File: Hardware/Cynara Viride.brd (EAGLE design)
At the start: 160 x 100 mm, 197 parts, among them Q1 TXC-7B, Q2 TXC-7WNEO, SW1 430181038816, SW2 , T1 PDTC143, T2 PDTC143, T3 PDTC143, T4 PDTC143, T5 PDTC143, U1 TM4C129EN, U2 MCP1826S 3V3, U3 LM4132 3V3, U4 XC6SLX9-3TQG, U5 M25P16-SO8, U6 MCP1826S 1V2, X1 EDGE 50p, X11 SOCK2X17, X12 SOCK2X17, X13 SOCK2X17, X2 EDGE 50p, X23 debug xilinx, X24 debug 10p, X3 EDGE 50p, X4 EDGE 50p, X5 MicroMatch 24, X6 , X7 SOCK2X17, X8 RJ45-LAN-10/100

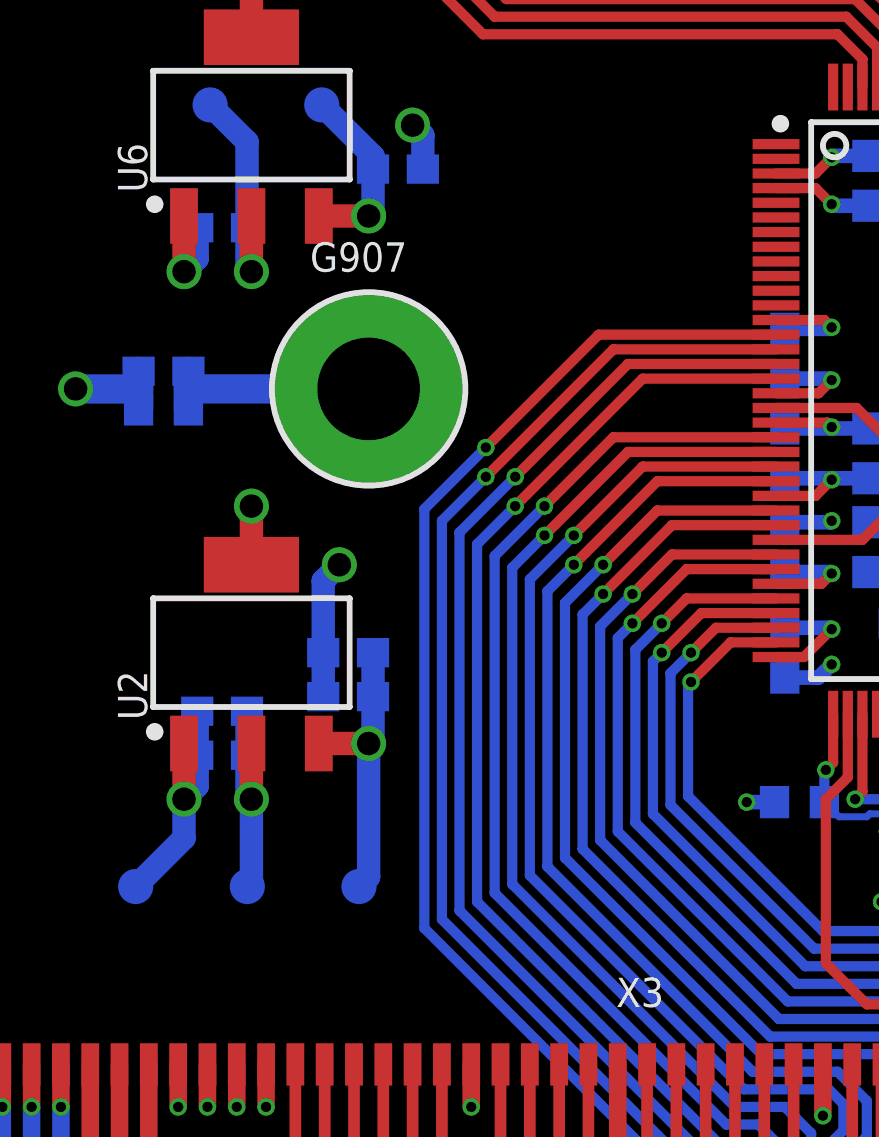
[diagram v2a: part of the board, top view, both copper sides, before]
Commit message: Added jumpers to disconnect the different power rails.
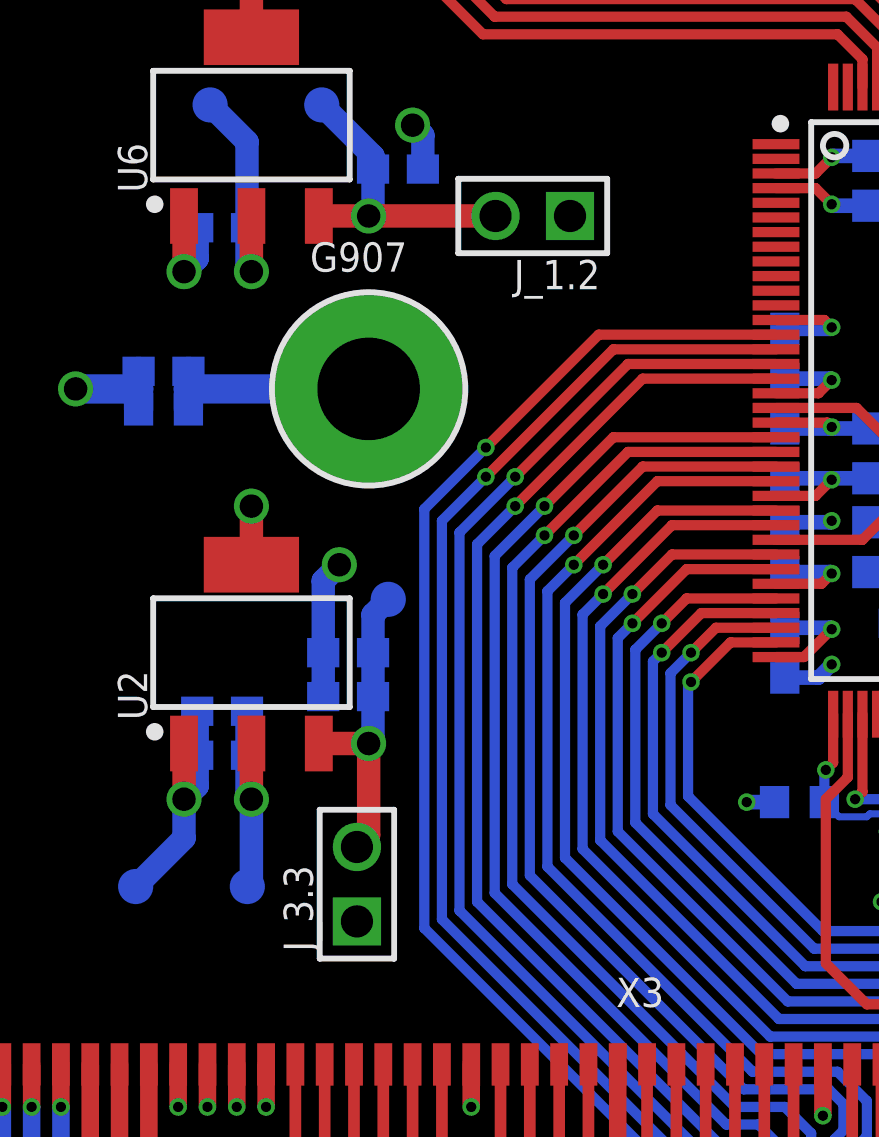
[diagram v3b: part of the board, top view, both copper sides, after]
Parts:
- added J_1.2, J_3.3: HDR1X2, Cynara-Connectors:1X2
- moved TP2 9.85 mm to (27.7, 42.8)
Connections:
- new net N$10: C44.1, J_1.2.2, TP3.1, U6.3
- new net N$7: C18.1, C57.1, J_3.3.2, TP2.1, U2.3
- net +1.2V: now also J_1.2.1; no longer C44.1, TP3.1, U6.3
- net +3.3V: now also J_3.3.1; no longer C18.1, C57.1, TP2.1, U2.3
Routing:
- net +1.2V: track 58.4 -> 44.6 mm, vias 5 -> 4
- net N$10: track 0.00 -> 10.6 mm, vias 0 -> 1
- net N$7: track 0.00 -> 10.6 mm, vias 0 -> 1
- net +3.3V: track 284.5 -> 274.6 mm, vias 49 -> 48
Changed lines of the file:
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@@
 <attribute name="XTRA" value="" x="19.05" y="33.02" size="1.778" layer="28" rot="MR0" display="off"/>
 </element>
-<element name="TP2" library="Cynara-Misc" package="TP-SMD" value=" " x="26.67" y="33.02" rot="MR0">
-<attribute name="Z" value="" x="26.67" y="33.02" size="1.778" layer="28" rot="MR0" display="off"/>
-<attribute name="WAARDE" value="" x="26.67" y="33.02" size="1.778" layer="28" rot="MR0" display="off"/>
-<attribute name="BEHUIZING" value="TP-EZ" x="26.67" y="33.02" size="1.778" layer="28" rot="MR0" display="off"/>
-<attribute name="ARTIKEL" value="" x="26.67" y="33.02" size="1.778" layer="28" rot="MR0" display="off"/>
-<attribute name="XTRA" value="" x="26.67" y="33.02" size="1.778" layer="28" rot="MR0" display="off"/>
+<element name="TP2" library="Cynara-Misc" package="TP-SMD" value=" " x="27.67" y="42.82" rot="MR0">
+<attribute name="Z" value="" x="27.67" y="42.82" size="1.778" layer="28" rot="MR0" display="off"/>
+<attribute name="WAARDE" value="" x="27.67" y="42.82" size="1.778" layer="28" rot="MR0" display="off"/>
+<attribute name="BEHUIZING" value="TP-EZ" x="27.67" y="42.82" size="1.778" layer="28" rot="MR0" display="off"/>
+<attribute name="ARTIKEL" value="" x="27.67" y="42.82" size="1.778" layer="28" rot="MR0" display="off"/>
+<attribute name="XTRA" value="" x="27.67" y="42.82" size="1.778" layer="28" rot="MR0" display="off"/>
 </element>
 <element name="TP3" library="Cynara-Misc" package="TP-SMD" value=" " x="25.4" y="59.69" rot="MR0">
@@
 <attribute name="MANUFACTURER" value="Texas Instruments" x="98.6" y="50" size="1.778" layer="27" rot="R315" display="off"/>
 </element>
+<element name="J_3.3" library="Cynara-Connectors" package="1X2" value="HDR1X2" x="26.6" y="33.1" rot="R90">
+<attribute name="MANUFACTURERPARTNO" value="61300211121" x="26.6" y="33.1" size="1.778" layer="27" rot="R90" display="off"/>
+<attribute name="MANUFACTURER" value="Wurth" x="26.6" y="33.1" size="1.778" layer="27" rot="R90" display="off"/>
+<attribute name="ORDERCODE" value="" x="26.6" y="33.1" size="1.778" layer="27" rot="R90" display="off"/>
+<attribute name="SUPPLIER" value="" x="26.6" y="33.1" size="1.778" layer="27" rot="R90" display="off"/>
+</element>
+<element name="J_1.2" library="Cynara-Connectors" package="1X2" value="HDR1X2" x="32.6" y="55.9" rot="R180">
+<attribute name="MANUFACTURERPARTNO" value="61300211121" x="32.6" y="55.9" size="1.778" layer="27" rot="R180" display="off"/>
+<attribute name="MANUFACTURER" value="Wurth" x="32.6" y="55.9" size="1.778" layer="27" rot="R180" display="off"/>
+<attribute name="ORDERCODE" value="" x="32.6" y="55.9" size="1.778" layer="27" rot="R180" display="off"/>
+<attribute name="SUPPLIER" value="" x="32.6" y="55.9" size="1.778" layer="27" rot="R180" display="off"/>
+</element>
 </elements>
 <signals>
@@
 <contactref element="C42" pad="1"/>
 <contactref element="L2" pad="2"/>
-<contactref element="C57" pad="1"/>
 <contactref element="R13" pad="2"/>
 <contactref element="C58" pad="1"/>
@@
 <wire x1="75.83" y1="16.3" x2="74" y2="18.13" width="0.35" layer="16"/>
 <wire x1="74" y1="18.13" x2="74" y2="24.2" width="0.35" layer="16"/>
-<contactref element="U2" pad="3"/>
-<contactref element="C18" pad="1"/>
 <contactref element="C61" pad="1"/>
 <contactref element="C62" pad="1"/>
@@
 <via x="80.6" y="36" extent="1-16" drill="0.35"/>
 <via x="44.7" y="34.9" extent="1-16" drill="0.35"/>
-<wire x1="25.3" y1="37.9" x2="27" y2="37.9" width="0.8" layer="1"/>
-<via x="27" y="37.9" extent="1-16" drill="0.8"/>
-<wire x1="27.15" y1="41" x2="27.15" y2="39.5" width="0.8" layer="16"/>
-<wire x1="27.15" y1="39.5" x2="27.15" y2="38.05" width="0.8" layer="16"/>
-<wire x1="27.15" y1="38.05" x2="27" y2="37.9" width="0.8" layer="16"/>
 <wire x1="46.46" y1="35.6" x2="45.4" y2="35.6" width="0.5" layer="1"/>
 <wire x1="45.4" y1="35.6" x2="44.7" y2="34.9" width="0.5" layer="1"/>
@@
 <wire x1="151" y1="78.15" x2="150.85" y2="78" width="0.35" layer="16"/>
 <wire x1="150.85" y1="78" x2="148" y2="78" width="0.35" layer="16"/>
-<contactref element="TP2" pad="1"/>
-<wire x1="26.67" y1="33.02" x2="27" y2="33.35" width="0.8" layer="16"/>
-<wire x1="27" y1="33.35" x2="27" y2="37.9" width="0.8" layer="16"/>
 <contactref element="U1" pad="7"/>
 <contactref element="U1" pad="16"/>
@@
 <wire x1="90.81715625" y1="57.5" x2="90.5" y2="57.5" width="0.24" layer="1"/>
 <via x="90.5" y="57.5" extent="1-16" drill="0.35"/>
+<contactref element="J_3.3" pad="1"/>
 </signal>
 <signal name="M0">
@@
 <vertex x="48" y="42"/>
 </polygon>
-<contactref element="U6" pad="3"/>
-<contactref element="C44" pad="1"/>
 <wire x1="62.3" y1="48.85" x2="61.35" y2="48.85" width="0.35" layer="1"/>
 <wire x1="61.35" y1="48.85" x2="61" y2="48.5" width="0.35" layer="1"/>
@@
 <wire x1="43.65" y1="49.35" x2="45.5" y2="47.5" width="0.35" layer="1"/>
 <wire x1="45.5" y1="47.5" x2="45.5" y2="46.5" width="0.35" layer="1"/>
-<wire x1="25.3" y1="55.9" x2="27" y2="55.9" width="0.8" layer="1"/>
-<via x="27" y="55.9" extent="1-16" drill="0.8"/>
-<wire x1="27.15" y1="57.5" x2="27.15" y2="56.05" width="0.8" layer="16"/>
-<wire x1="27.15" y1="56.05" x2="27" y2="55.9" width="0.8" layer="16"/>
-<wire x1="27" y1="55.9" x2="41.1" y2="55.9" width="0.8" layer="15"/>
-<wire x1="41.1" y1="55.9" x2="44" y2="53" width="0.8" layer="15"/>
-<contactref element="TP3" pad="1"/>
-<wire x1="25.4" y1="59.69" x2="27.15" y2="57.94" width="0.8" layer="16"/>
-<wire x1="27.15" y1="57.94" x2="27.15" y2="57.5" width="0.8" layer="16"/>
+<contactref element="J_1.2" pad="1"/>
+<wire x1="33.87" y1="55.9" x2="41" y2="55.9" width="0.8" layer="15"/>
+<wire x1="41" y1="55.9" x2="43.5" y2="53.4" width="0.8" layer="15"/>
 </signal>
 <signal name="X3V3">
@@
 <wire x1="102.7" y1="58.908328125" x2="102.7" y2="59" width="0.24" layer="1"/>
 </signal>
+<signal name="N$7">
+<contactref element="C57" pad="1"/>
+<contactref element="U2" pad="3"/>
+<contactref element="C18" pad="1"/>
+<contactref element="TP2" pad="1"/>
+<contactref element="J_3.3" pad="2"/>
+<wire x1="25.3" y1="37.9" x2="27" y2="37.9" width="0.8" layer="1"/>
+<via x="27" y="37.9" extent="1-16" drill="0.8"/>
+<wire x1="27.15" y1="41" x2="27.15" y2="39.5" width="0.8" layer="16"/>
+<wire x1="27.15" y1="39.5" x2="27.15" y2="38.05" width="0.8" layer="16"/>
+<wire x1="27.15" y1="38.05" x2="27" y2="37.9" width="0.8" layer="16"/>
+<wire x1="26.6" y1="34.37" x2="27" y2="34.77" width="0.8" layer="1"/>
+<wire x1="27" y1="34.77" x2="27" y2="37.9" width="0.8" layer="1"/>
+<wire x1="27.15" y1="41" x2="27.15" y2="42.3" width="0.8" layer="16"/>
+<wire x1="27.15" y1="42.3" x2="27.67" y2="42.82" width="0.8" layer="16"/>
+</signal>
+<signal name="N$10">
+<contactref element="U6" pad="3"/>
+<contactref element="C44" pad="1"/>
+<contactref element="TP3" pad="1"/>
+<contactref element="J_1.2" pad="2"/>
+<wire x1="25.3" y1="55.9" x2="27" y2="55.9" width="0.8" layer="1"/>
+<via x="27" y="55.9" extent="1-16" drill="0.8"/>
+<wire x1="27.15" y1="57.5" x2="27.15" y2="56.05" width="0.8" layer="16"/>
+<wire x1="27.15" y1="56.05" x2="27" y2="55.9" width="0.8" layer="16"/>
+<wire x1="25.4" y1="59.69" x2="27.15" y2="57.94" width="0.8" layer="16"/>
+<wire x1="27.15" y1="57.94" x2="27.15" y2="57.5" width="0.8" layer="16"/>
+<wire x1="31.33" y1="55.9" x2="27" y2="55.9" width="0.8" layer="1"/>
+</signal>
 </signals>

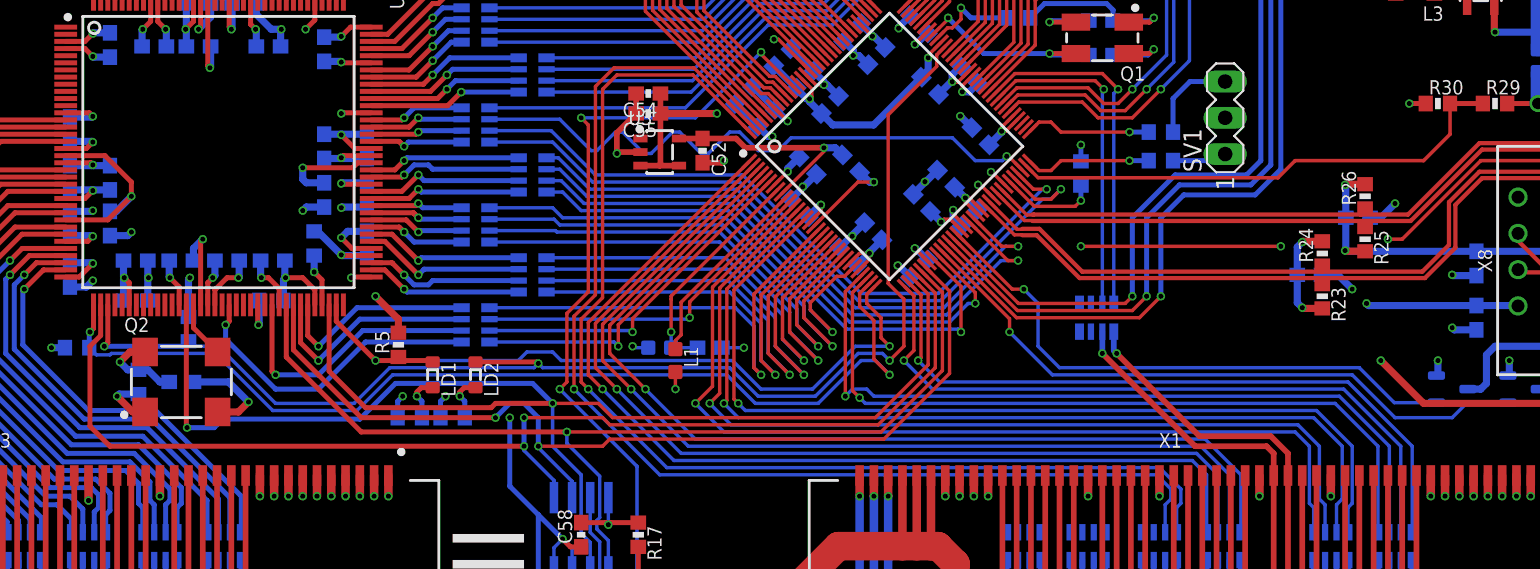
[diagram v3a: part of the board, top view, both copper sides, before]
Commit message: Added more test points.
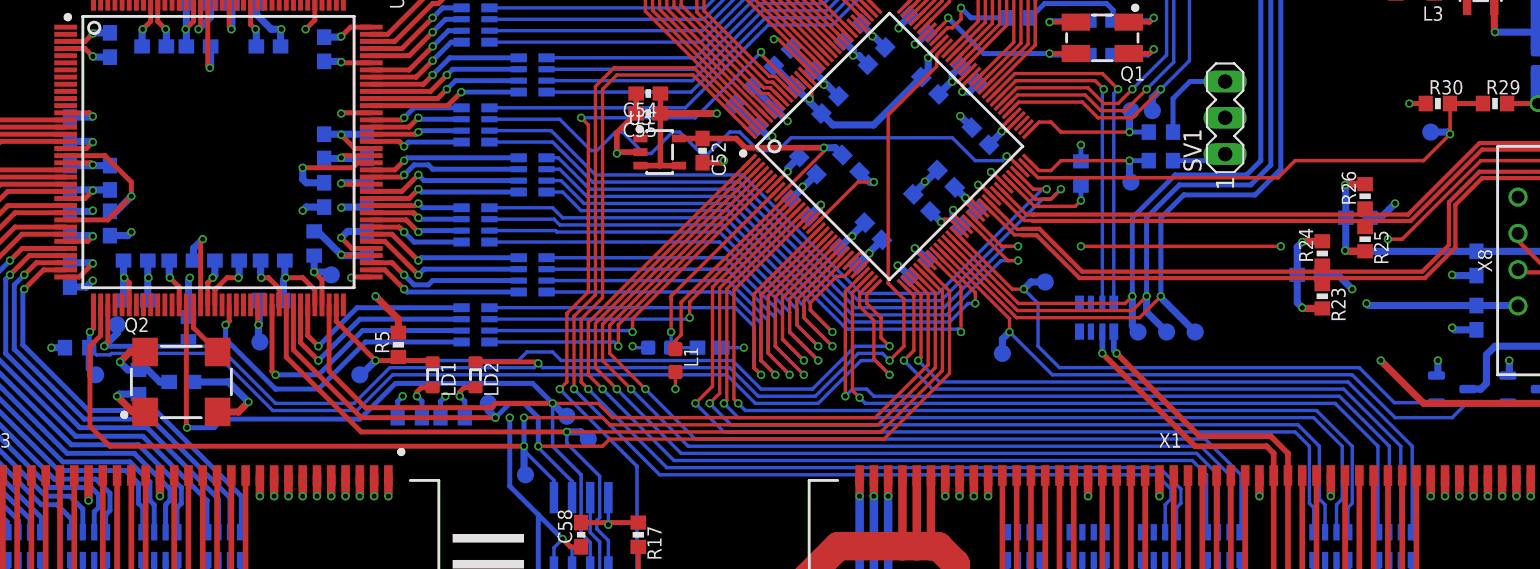
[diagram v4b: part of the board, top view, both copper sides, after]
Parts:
- added TP10, TP12, TP13, TP14, TP15, TP16, TP17, TP18, TP19, TP20, TP21, TP22, TP23, TP24, TP6, TP7, TP8, TP9: (no value), Cynara-Misc:TP-SMD
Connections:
- net !HIB: now also TP8.1
- net !RST: now also TP6.1
- net !WAKE: now also TP7.1
- net DONE: now also TP21.1
- net INIT: now also TP20.1
- net M0: now also TP10.1
- net M1: now also TP9.1
- net PF0_ETH: now also TP24.1
- net PF1_LEDR: now also TP16.1
- net PF2_LEDB: now also TP18.1
- net PF3_LEDG: now also TP17.1
- net PF4_ETH: now also TP23.1
- net PROGRAM: now also TP19.1
- net SSI0CLK: now also TP12.1
- net SSI0D0: now also TP13.1
- net SSI0D1: now also TP14.1
- net SSI0FSS: now also TP15.1
- net USB_DETECT: now also TP22.1
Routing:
- net PF1_LEDR: track 61.7 -> 65.2 mm
- net PF2_LEDB: track 56.1 -> 59.2 mm
- net PF3_LEDG: track 51.1 -> 53.8 mm
- net PROGRAM: track 72.2 -> 74.3 mm
- net SSI0FSS: track 84.0 -> 86.0 mm
- net INIT: track 92.5 -> 94.3 mm
- net !RST: track 78.2 -> 80.0 mm
- net SSI0D0: track 72.4 -> 74.1 mm
- net PF4_ETH: track 40.2 -> 41.9 mm
- net PF0_ETH: track 45.5 -> 47.2 mm
- net !WAKE: track 8.87 -> 10.4 mm
- net !HIB: track 8.88 -> 10.4 mm
- net DONE: track 52.9 -> 54.4 mm
- net USB_DETECT: track 35.8 -> 37.2 mm, vias 0 -> 1
- net SSI0CLK: track 105.2 -> 106.6 mm
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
